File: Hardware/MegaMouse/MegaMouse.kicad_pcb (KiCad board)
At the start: 2 copper layers, 94 x 99 mm, 8 parts, among them J101 MotorL, J102 MotorR, U101 ATmega328P-A

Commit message: Bump libs
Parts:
- moved BT101 192.9 mm to (-35.5, 34.0)
- moved D101 192.9 mm to (-44.0, 36.7)
- moved D102 192.9 mm to (41.8, 36.7)
- moved D103 192.9 mm to (-44.0, 31.8)
- moved D104 192.9 mm to (41.8, 31.8)
- moved J101 192.9 mm to (-10.0, 0.00)
- moved J102 192.9 mm to (10.0, 0.00)
- moved U101 192.9 mm to (0.00, -20.0)
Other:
- board text added: "Maze Cell"
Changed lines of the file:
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@@
   (net 49 "unconnected-(D104-Pad2)")
   (footprint "LED_THT:LED_D3.0mm_Horizontal_O6.35mm_Z6.0mm" (layer "F.Cu")
-    (at 121 131.8)
+    (at -44 31.8)
     (descr "LED, diameter 3.0mm z-position of LED center 2.0mm, 2 pins, diameter 3.0mm z-position of LED center 2.0mm, 2 pins, diameter 3.0mm z-position of LED center 2.0mm, 2 pins, diameter 3.0mm z-position of LED center 6.0mm, 2 pins, diameter 3.0mm z-position of LED center 6.0mm, 2 pins, diameter 3.0mm z-position of LED center 6.0mm, 2 pins")
     (tags "LED diameter 3.0mm z-position of LED center 2.0mm 2 pins diameter 3.0mm z-position of LED center 2.0mm 2 pins diameter 3.0mm z-position of LED center 2.0mm 2 pins diameter 3.0mm z-position of LED center 6.0mm 2 pins diameter 3.0mm z-position of LED center 6.0mm 2 pins diameter 3.0mm z-position of LED center 6.0mm 2 pins")
@@
   )
   (footprint "LED_THT:LED_D3.0mm_Horizontal_O1.27mm_Z2.0mm" (layer "F.Cu")
-    (at 121 136.675)
+    (at -44 36.675)
     (descr "LED, diameter 3.0mm z-position of LED center 2.0mm, 2 pins")
     (tags "LED diameter 3.0mm z-position of LED center 2.0mm 2 pins")
@@
   )
   (footprint "MegaMouse:MicroMotor" (layer "F.Cu")
-    (at 155 100)
+    (at -10 0)
     (property "Sheetfile" "MegaMouse.kicad_sch")
     (property "Sheetname" "")
@@
   )
   (footprint "MegaMouse:MicroMotor" (layer "F.Cu")
-    (at 175 100 180)
+    (at 10 0 180)
     (property "Sheetfile" "MegaMouse.kicad_sch")
     (property "Sheetname" "")
@@
   )
   (footprint "LED_THT:LED_D3.0mm_Horizontal_O6.35mm_Z6.0mm" (layer "F.Cu")
-    (at 206.75 131.8)
+    (at 41.75 31.8)
     (descr "LED, diameter 3.0mm z-position of LED center 2.0mm, 2 pins, diameter 3.0mm z-position of LED center 2.0mm, 2 pins, diameter 3.0mm z-position of LED center 2.0mm, 2 pins, diameter 3.0mm z-position of LED center 6.0mm, 2 pins, diameter 3.0mm z-position of LED center 6.0mm, 2 pins, diameter 3.0mm z-position of LED center 6.0mm, 2 pins")
     (tags "LED diameter 3.0mm z-position of LED center 2.0mm 2 pins diameter 3.0mm z-position of LED center 2.0mm 2 pins diameter 3.0mm z-position of LED center 2.0mm 2 pins diameter 3.0mm z-position of LED center 6.0mm 2 pins diameter 3.0mm z-position of LED center 6.0mm 2 pins diameter 3.0mm z-position of LED center 6.0mm 2 pins")
@@
   )
   (footprint "LED_THT:LED_D3.0mm_Horizontal_O1.27mm_Z2.0mm" (layer "F.Cu")
-    (at 206.75 136.675)
+    (at 41.75 36.675)
     (descr "LED, diameter 3.0mm z-position of LED center 2.0mm, 2 pins")
     (tags "LED diameter 3.0mm z-position of LED center 2.0mm 2 pins")
@@
   )
   (footprint "Battery:BatteryHolder_MPD_BH-18650-PC2" (layer "F.Cu")
-    (at 129.5 134)
+    (at -35.5 34)
     (descr "18650 Battery Holder (http://www.memoryprotectiondevices.com/datasheets/BK-18650-PC2-datasheet.pdf)")
     (tags "18650 Battery Holder")
@@
   )
   (footprint "Package_QFP:TQFP-32_7x7mm_P0.8mm" (layer "F.Cu")
-    (at 165 80 45)
+    (at 0 -20 45)
     (descr "32-Lead Plastic Thin Quad Flatpack (PT) - 7x7x1.0 mm Body, 2.00 mm [TQFP] (see Microchip Packaging Specification 00000049BS.pdf)")
     (tags "QFP 0.8")
@@
     )
   )
-  (gr_rect (start 212 145) (end 118 46) (layer "Dwgs.User") (width 0.15) (fill none))
-  (gr_rect locked (start 75 25) (end 235 185) (layer "Cmts.User") (width 0.15) (fill none))
-  (gr_arc (start 165 46) (mid 190.558788 52.264773) (end 210 70) (layer "Edge.Cuts") (width 0.1))
-  (gr_arc (start 119 82) (mid 118.292896 81.707106) (end 118 81) (layer "Edge.Cuts") (width 0.1))
-  (gr_arc (start 129 117) (mid 128.707107 117.707107) (end 128 118) (layer "Edge.Cuts") (width 0.1))
-  (gr_arc (start 120 70) (mid 139.441212 52.264773) (end 165 46) (layer "Edge.Cuts") (width 0.1))
-  (gr_line (start 210 119) (end 212 144.5) (layer "Edge.Cuts") (width 0.1))
-  (gr_line (start 121 118) (end 128 118) (layer "Edge.Cuts") (width 0.1))
-  (gr_line (start 119 82) (end 128 82) (layer "Edge.Cuts") (width 0.1))
-  (gr_arc (start 128 82) (mid 128.707109 82.292892) (end 129 83) (layer "Edge.Cuts") (width 0.1))
-  (gr_line (start 202 118) (end 209 118) (layer "Edge.Cuts") (width 0.1))
-  (gr_line (start 118.5 145) (end 211.5 145) (layer "Edge.Cuts") (width 0.1))
-  (gr_arc (start 212 81) (mid 211.707107 81.707107) (end 211 82) (layer "Edge.Cuts") (width 0.1))
-  (gr_arc (start 209 118) (mid 209.707107 118.292893) (end 210 119) (layer "Edge.Cuts") (width 0.1))
-  (gr_arc (start 201 83) (mid 201.292893 82.292893) (end 202 82) (layer "Edge.Cuts") (width 0.1))
-  (gr_line (start 202 82) (end 211 82) (layer "Edge.Cuts") (width 0.1))
-  (gr_line (start 118 144.5) (end 120 119) (layer "Edge.Cuts") (width 0.1))
-  (gr_line (start 129 83) (end 129 117) (layer "Edge.Cuts") (width 0.1))
-  (gr_line (start 201 117) (end 201 83) (layer "Edge.Cuts") (width 0.1))
-  (gr_arc (start 212 144.5) (mid 211.853553 144.853553) (end 211.5 145) (layer "Edge.Cuts") (width 0.1))
-  (gr_arc (start 118.5 145) (mid 118.146447 144.853553) (end 118 144.5) (layer "Edge.Cuts") (width 0.1))
-  (gr_arc (start 210 70) (mid 211.429022 75.421996) (end 212 81) (layer "Edge.Cuts") (width 0.1))
-  (gr_arc (start 202 118) (mid 201.292893 117.707107) (end 201 117) (layer "Edge.Cuts") (width 0.1))
-  (gr_arc (start 118 81) (mid 118.570978 75.421996) (end 120 70) (layer "Edge.Cuts") (width 0.1))
-  (gr_arc (start 120 119) (mid 120.292893 118.292893) (end 121 118) (layer "Edge.Cuts") (width 0.1))
+  (gr_rect (start 47 45) (end -47 -54) (layer "Dwgs.User") (width 0.15) (fill none))
+  (gr_rect locked (start 80 80) (end -80 -80) (layer "Cmts.User") (width 0.15) (fill none))
+  (gr_arc (start 0 -54) (mid 25.558789 -47.735228) (end 45 -30) (layer "Edge.Cuts") (width 0.1))
+  (gr_arc (start -46 -18) (mid -46.707107 -18.292893) (end -47 -19) (layer "Edge.Cuts") (width 0.1))
+  (gr_arc (start -36 17) (mid -36.292893 17.707107) (end -37 18) (layer "Edge.Cuts") (width 0.1))
+  (gr_arc (start -45 -30) (mid -25.558787 -47.735225) (end 0 -54) (layer "Edge.Cuts") (width 0.1))
+  (gr_line (start 45 19) (end 47 44.5) (layer "Edge.Cuts") (width 0.1))
+  (gr_line (start -44 18) (end -37 18) (layer "Edge.Cuts") (width 0.1))
+  (gr_line (start -46 -18) (end -37 -18) (layer "Edge.Cuts") (width 0.1))
+  (gr_arc (start -37 -18) (mid -36.292893 -17.707107) (end -36 -17) (layer "Edge.Cuts") (width 0.1))
+  (gr_line (start 37 18) (end 44 18) (layer "Edge.Cuts") (width 0.1))
+  (gr_line (start -46.5 45) (end 46.5 45) (layer "Edge.Cuts") (width 0.1))
+  (gr_arc (start 47 -19) (mid 46.707107 -18.292893) (end 46 -18) (layer "Edge.Cuts") (width 0.1))
+  (gr_arc (start 44 18) (mid 44.707107 18.292893) (end 45 19) (layer "Edge.Cuts") (width 0.1))
+  (gr_arc (start 36 -17) (mid 36.292893 -17.707107) (end 37 -18) (layer "Edge.Cuts") (width 0.1))
+  (gr_line (start 37 -18) (end 46 -18) (layer "Edge.Cuts") (width 0.1))
+  (gr_line (start -47 44.5) (end -45 19) (layer "Edge.Cuts") (width 0.1))
+  (gr_line (start -36 -17) (end -36 17) (layer "Edge.Cuts") (width 0.1))
+  (gr_line (start 36 17) (end 36 -17) (layer "Edge.Cuts") (width 0.1))
+  (gr_arc (start 47 44.5) (mid 46.853553 44.853553) (end 46.5 45) (layer "Edge.Cuts") (width 0.1))
+  (gr_arc (start -46.5 45) (mid -46.853553 44.853553) (end -47 44.5) (layer "Edge.Cuts") (width 0.1))
+  (gr_arc (start 45 -30) (mid 46.429018 -24.578004) (end 47 -19) (layer "Edge.Cuts") (width 0.1))
+  (gr_arc (start 37 18) (mid 36.292893 17.707107) (end 36 17) (layer "Edge.Cuts") (width 0.1))
+  (gr_arc (start -47 -19) (mid -46.429026 -24.578005) (end -45 -30) (layer "Edge.Cuts") (width 0.1))
+  (gr_arc (start -45 19) (mid -44.707107 18.292893) (end -44 18) (layer "Edge.Cuts") (width 0.1))
+  (gr_text "Maze Cell" (at -69.5 -82) (layer "Cmts.User")
+    (effects (font (size 3 3) (thickness 0.15)))
+  )
+  (dimension (type aligned) (layer "Cmts.User")
+    (pts (xy 80 80) (xy 80 -80))
+    (height 2.5)
+    (gr_text "160.0000 mm" (at 81.35 0 90) (layer "Cmts.User")
+      (effects (font (size 1 1) (thickness 0.15)))
+    )
+    (format (units 3) (units_format 1) (precision 4))
+    (style (thickness 0.15) (arrow_length 1.27) (text_position_mode 0) (extension_height 0.58642) (extension_offset 0.5) keep_text_aligned)
+  )
+  (dimension (type aligned) (layer "Cmts.User")
+    (pts (xy 80 80) (xy -80 80))
+    (height -2.5)
+    (gr_text "160.0000 mm" (at 0 81.35) (layer "Cmts.User")
+      (effects (font (size 1 1) (thickness 0.15)))
+    )
+    (format (units 3) (units_format 1) (precision 4))
+    (style (thickness 0.15) (arrow_length 1.27) (text_position_mode 0) (extension_height 0.58642) (extension_offset 0.5) keep_text_aligned)
+  )
 )

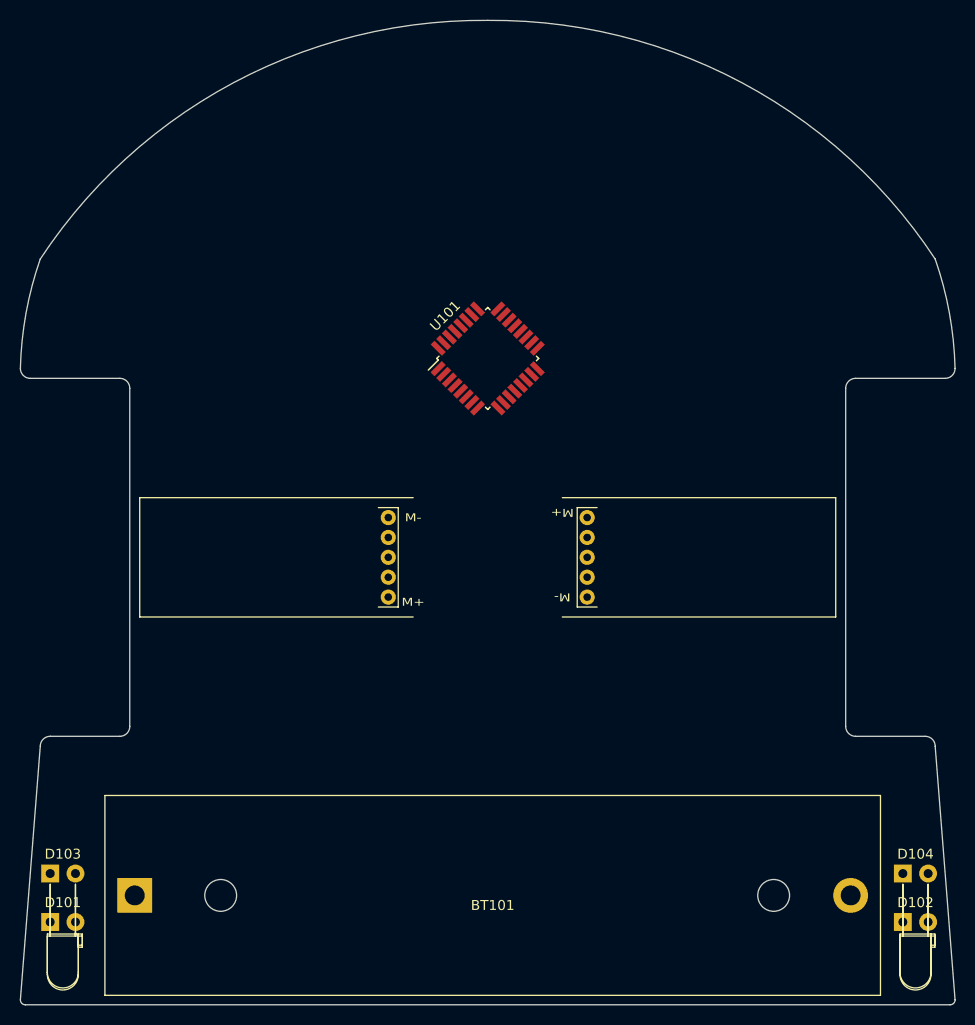
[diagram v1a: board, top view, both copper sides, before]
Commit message: Add brakelight as full kicad_mod
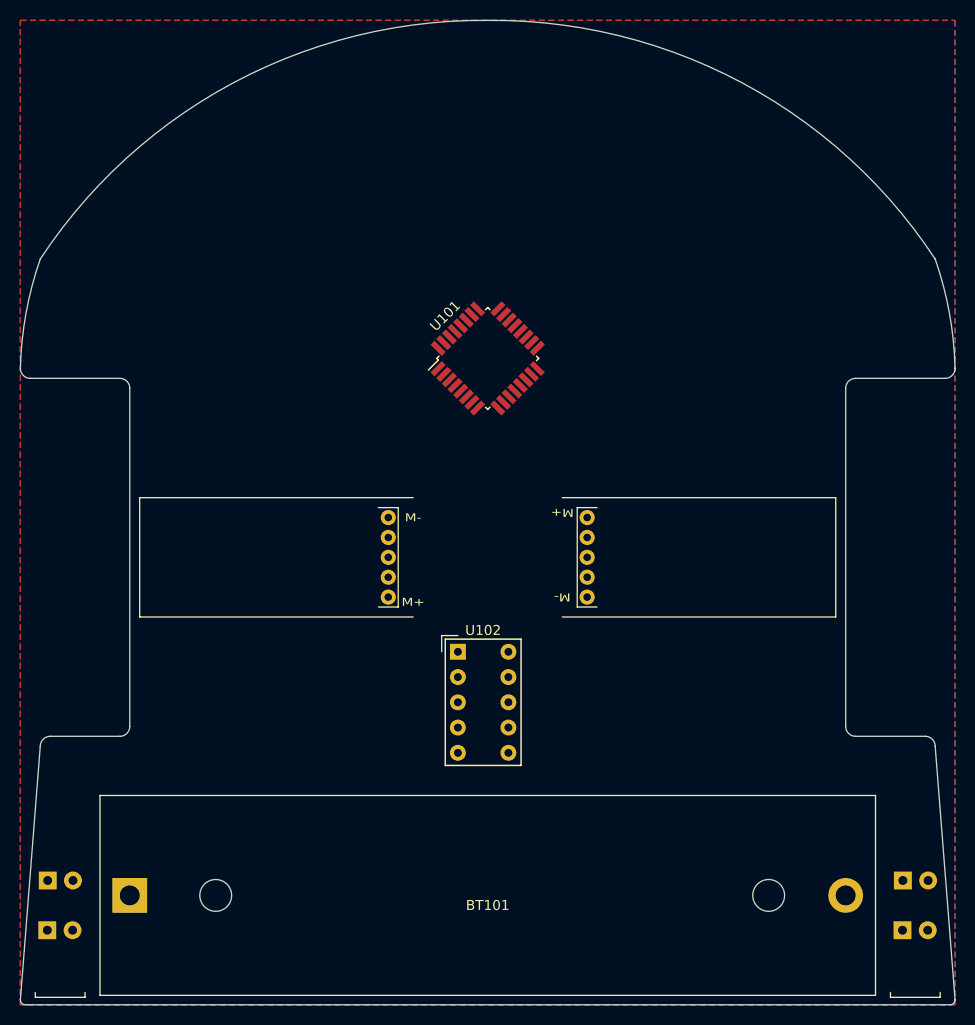
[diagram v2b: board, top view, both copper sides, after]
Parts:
- removed D103: TurnL, LED_THT:LED_D3.0mm_Horizontal_O6.35mm_Z6.0mm
- removed D104: TurnR, LED_THT:LED_D3.0mm_Horizontal_O6.35mm_Z6.0mm
- added U102: HDSP-7803, Display_7Segment:HDSP-7801, F.Cu at (-3.00, 9.50)
- D101: value BrakeLight -> LeftTail; footprint LED_THT:LED_D3.0mm_Horizontal_O1.27mm_Z2.0mm -> MegaMouse:BrakeLight
- D102: value BrakeLight -> RightTail; footprint LED_THT:LED_D3.0mm_Horizontal_O1.27mm_Z2.0mm -> MegaMouse:BrakeLight
- moved D102 1.50 mm to (43.0, 37.5)
- moved D101 1.30 mm to (-43.0, 37.5)
- moved BT101 0.50 mm to (-36.0, 34.0)
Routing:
- added copper zone on B.Cu, net GND
- added copper zone on F.Cu, net GND

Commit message: Make awesome
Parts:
- removed J101: MotorL, MegaMouse:MicroMotor
- removed J102: MotorR, MegaMouse:MicroMotor
- added BT102: Cell2, Battery:BatteryHolder_MPD_BH-18650-PC2, F.Cu at (-36.0, 55.5)
- added C201: 10uf, Capacitor_SMD:CP_Elec_4x3, F.Cu at (-25.5, -25.9)
- added C301: 10uf, Capacitor_SMD:CP_Elec_4x3, F.Cu at (25.5, -25.6)
- added J201: Motor, MegaMouse:MicroMotor, F.Cu at (-9.50, 0.00)
- added J301: Motor, MegaMouse:MicroMotor, F.Cu at (9.50, 0.00)
- added U201: DRV8871DDA, Package_SO:Texas_HTSOP-8-1EP_3.9x4.9mm_P1.27mm_EP2.95x4.9mm_Mask2.4x3.1mm_ThermalVias, F.Cu at (-28.5, -19.5)
- added U301: DRV8871DDA, Package_SO:Texas_HTSOP-8-1EP_3.9x4.9mm_P1.27mm_EP2.95x4.9mm_Mask2.4x3.1mm_ThermalVias, F.Cu at (28.5, -19.1)
- BT101: value Battery_Cell -> Cell1
- moved D101 20.5 mm to (-43.0, 58.0)
- moved D102 20.5 mm to (43.0, 58.0)
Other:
- board size 94 x 99 mm -> 94 x 120.5 mm

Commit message: Clean board
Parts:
- U102: value HDSP-7803 -> STATE
- moved U102 50.3 mm to (-2.47, -40.8)
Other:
- board size 94 x 120.5 mm -> 93 x 120.5 mm
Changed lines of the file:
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@@
   )
   (footprint "Display_7Segment:HDSP-7801" (layer "F.Cu")
-    (at -3 9.5)
+    (at -2.4675 -40.7675)
     (descr "One digit 7 segment green, https://docs.broadcom.com/docs/AV02-2553EN")
     (tags "One digit 7 segment green")
@@
     (property "Sheetname" "")
     (attr through_hole)
-    (fp_text reference "U102" (at 2.54 -2.159) (layer "F.SilkS")
-      (effects (font (size 1 1) (thickness 0.15)))
-    )
-    (fp_text value "HDSP-7803" (at 2.54 12.7) (layer "F.Fab")
+    (fp_text reference "U102" (at 2.54 -2.159) (layer "F.SilkS") hide
+      (effects (font (size 1 1) (thickness 0.15)))
+    )
+    (fp_text value "STATE" (at 2.54 -2.4825) (layer "F.SilkS")
       (effects (font (size 1 1) (thickness 0.15)))
     )
@@
     )
   )
-  (gr_rect (start 47 66.5) (end -47 -54) (layer "Dwgs.User") (width 0.15) (fill none))
+  (gr_rect (start 46.5 66.5) (end -46.5 -54) (layer "Dwgs.User") (width 0.15) (fill none))
   (gr_rect locked (start 80 80) (end -80 -80) (layer "Cmts.User") (width 0.15) (fill none))
-  (gr_arc (start 0 -54) (mid 25.558789 -47.735228) (end 45 -30) (layer "Edge.Cuts") (width 0.1))
-  (gr_arc (start -46 -18) (mid -46.707107 -18.292893) (end -47 -19) (layer "Edge.Cuts") (width 0.1))
-  (gr_arc (start -36 17) (mid -36.292893 17.707107) (end -37 18) (layer "Edge.Cuts") (width 0.1))
-  (gr_arc (start -45 -30) (mid -25.558787 -47.735225) (end 0 -54) (layer "Edge.Cuts") (width 0.1))
-  (gr_line (start 47 19) (end 47 66) (layer "Edge.Cuts") (width 0.1))
-  (gr_line (start -46 18) (end -37 18) (layer "Edge.Cuts") (width 0.1))
-  (gr_line (start -46 -18) (end -37 -18) (layer "Edge.Cuts") (width 0.1))
-  (gr_arc (start -37 -18) (mid -36.292893 -17.707107) (end -36 -17) (layer "Edge.Cuts") (width 0.1))
-  (gr_line (start 37 18) (end 46 18) (layer "Edge.Cuts") (width 0.1))
-  (gr_line (start -46.5 66.5) (end 46.5 66.5) (layer "Edge.Cuts") (width 0.1))
-  (gr_arc (start 47 -19) (mid 46.707107 -18.292893) (end 46 -18) (layer "Edge.Cuts") (width 0.1))
-  (gr_line (start -47 19) (end -47 66) (layer "Edge.Cuts") (width 0.1))
-  (gr_arc (start 46 18) (mid 46.707107 18.292893) (end 47 19) (layer "Edge.Cuts") (width 0.1))
-  (gr_arc (start 36 -17) (mid 36.292893 -17.707107) (end 37 -18) (layer "Edge.Cuts") (width 0.1))
-  (gr_line (start 37 -18) (end 46 -18) (layer "Edge.Cuts") (width 0.1))
-  (gr_line (start -36 -17) (end -36 17) (layer "Edge.Cuts") (width 0.1))
-  (gr_arc (start -47 19) (mid -46.707107 18.292893) (end -46 18) (layer "Edge.Cuts") (width 0.1))
-  (gr_line (start 36 17) (end 36 -17) (layer "Edge.Cuts") (width 0.1))
-  (gr_arc (start 47 66) (mid 46.853553 66.353553) (end 46.5 66.5) (layer "Edge.Cuts") (width 0.1))
-  (gr_arc (start -46.5 66.5) (mid -46.853553 66.353553) (end -47 66) (layer "Edge.Cuts") (width 0.1))
-  (gr_arc (start 45 -30) (mid 46.429018 -24.578004) (end 47 -19) (layer "Edge.Cuts") (width 0.1))
-  (gr_arc (start 37 18) (mid 36.292893 17.707107) (end 36 17) (layer "Edge.Cuts") (width 0.1))
-  (gr_arc (start -47 -19) (mid -46.429026 -24.578005) (end -45 -30) (layer "Edge.Cuts") (width 0.1))
+  (gr_arc (start 0 -54) (mid 27.881729 -45.811488) (end 46.5 -23.5) (layer "Edge.Cuts") (width 0.1))
+  (gr_line (start -46.5 -21.25) (end -46.5 -23.5) (layer "Edge.Cuts") (width 0.1))
+  (gr_line (start 46.5 21.25) (end 46.5 65.5) (layer "Edge.Cuts") (width 0.1))
+  (gr_arc (start -46.5 -23.5) (mid -27.881729 -45.811488) (end 0 -54) (layer "Edge.Cuts") (width 0.1))
+  (gr_line (start 37 21.25) (end 46.5 21.25) (layer "Edge.Cuts") (width 0.1))
+  (gr_line (start -45.5 66.5) (end 45.5 66.5) (layer "Edge.Cuts") (width 0.1))
+  (gr_arc (start -36 20.25) (mid -36.292893 20.957107) (end -37 21.25) (layer "Edge.Cuts") (width 0.1))
+  (gr_line (start -46.5 21.25) (end -37 21.25) (layer "Edge.Cuts") (width 0.1))
+  (gr_arc (start -37 -21.25) (mid -36.280223 -20.969777) (end -36 -20.25) (layer "Edge.Cuts") (width 0.1))
+  (gr_line (start -46.5 21.25) (end -46.5 65.5) (layer "Edge.Cuts") (width 0.1))
+  (gr_line (start -36 -20.25) (end -36 20.25) (layer "Edge.Cuts") (width 0.1))
+  (gr_arc (start 36 -20.25) (mid 36.280223 -20.969777) (end 37 -21.25) (layer "Edge.Cuts") (width 0.1))
+  (gr_arc (start -45.5 66.5) (mid -46.207107 66.207107) (end -46.5 65.5) (layer "Edge.Cuts") (width 0.1))
+  (gr_line (start 37 -21.25) (end 46.5 -21.25) (layer "Edge.Cuts") (width 0.1))
+  (gr_line (start -46.5 -21.25) (end -37 -21.25) (layer "Edge.Cuts") (width 0.1))
+  (gr_line (start 46.5 -23.5) (end 46.5 -21.25) (layer "Edge.Cuts") (width 0.1))
+  (gr_line (start 36 20.25) (end 36 -20.25) (layer "Edge.Cuts") (width 0.1))
+  (gr_arc (start 37 21.25) (mid 36.292893 20.957107) (end 36 20.25) (layer "Edge.Cuts") (width 0.1))
+  (gr_arc (start 46.5 65.5) (mid 46.207107 66.207107) (end 45.5 66.5) (layer "Edge.Cuts") (width 0.1))
   (gr_text "Maze Cell" (at -69.5 -82) (layer "Cmts.User")
     (effects (font (size 3 3) (thickness 0.15)))
@@
     (polygon
       (pts
-        (xy 47 66.5)
-        (xy -47 66.5)
-        (xy -47 -54)
-        (xy 47 -54)
+        (xy 46.5 66.5)
+        (xy -46.5 66.5)
+        (xy -46.5 -54)
+        (xy 46.5 -54)
       )
     )
